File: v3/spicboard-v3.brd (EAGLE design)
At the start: 65 x 60 mm, 40 parts, among them IC1 74HC595, Q1 BC557, Q2 BC557

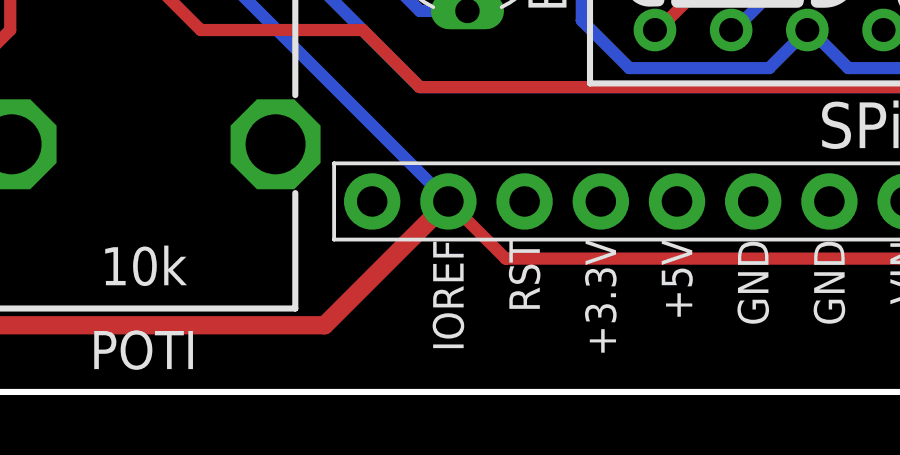
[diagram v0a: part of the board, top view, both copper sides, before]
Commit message: IOREF nach VCC umbenannt
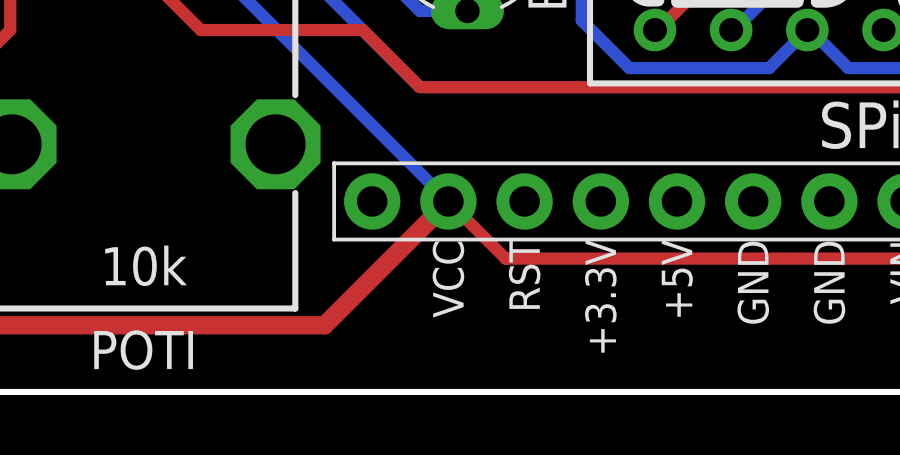
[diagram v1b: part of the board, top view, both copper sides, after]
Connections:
- net VCC: now also B1.VCC; no longer B1.IOREF
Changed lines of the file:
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@@
 <wire x1="2.794" y1="3.556" x2="4.1275" y2="2.2225" width="0.6096" layer="1"/>
 <wire x1="2.794" y1="3.556" x2="2.794" y2="4.191" width="0.6096" layer="1"/>
-<contactref element="B1" pad="IOREF"/>
+<contactref element="B1" pad="VCC"/>
 <wire x1="16.495" y1="15.255" x2="16.51" y2="15.24" width="0.4064" layer="16"/>
 <wire x1="16.51" y1="15.24" x2="16.51" y2="13.97" width="0.4064" layer="16"/>

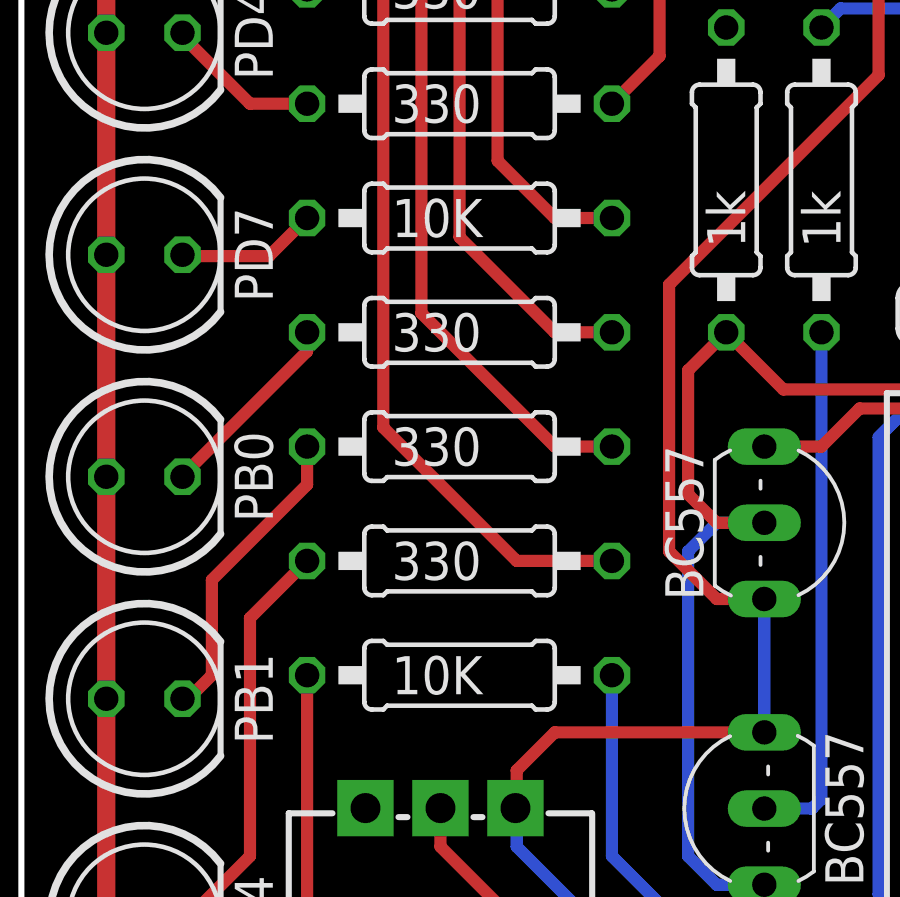
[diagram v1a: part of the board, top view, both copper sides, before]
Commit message: SPiCboard: 10K -> 10k
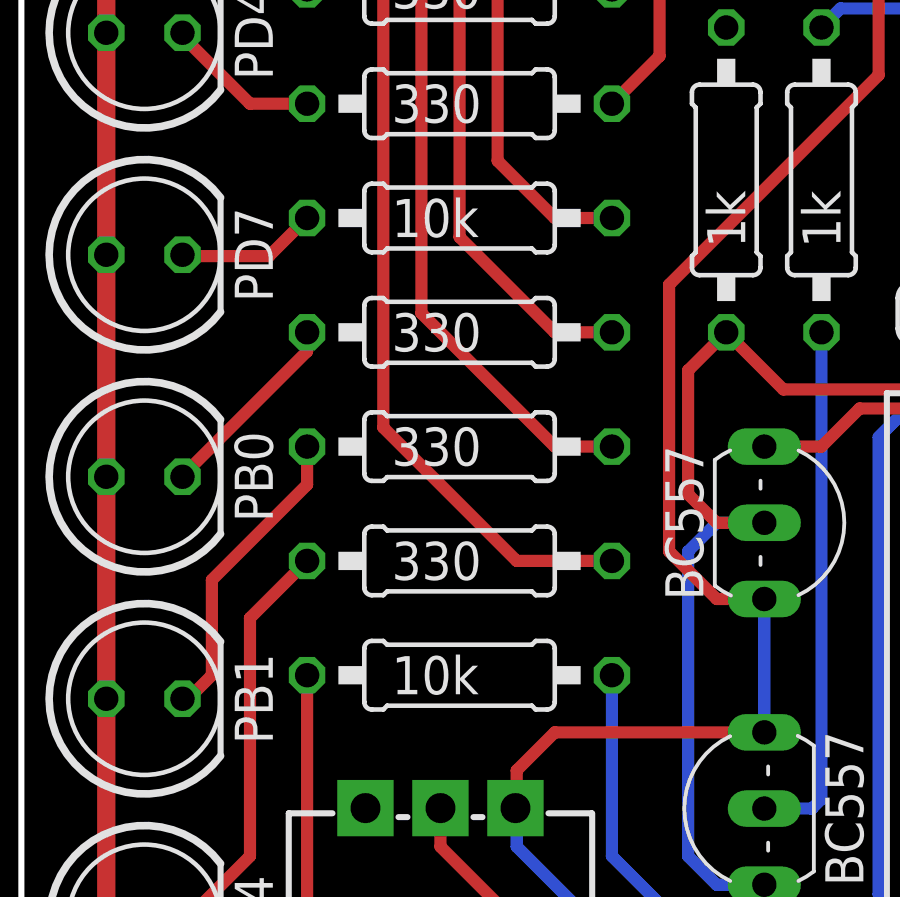
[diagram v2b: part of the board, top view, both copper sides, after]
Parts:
- R4, R8: value 10K -> 10k
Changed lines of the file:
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@@
 <attribute name="VALUE" x="12.3444" y="38.1" size="1.27" layer="25" ratio="10"/>
 </element>
-<element name="R4" library="resistor" package="0207/10" value="10K" x="14.605" y="34.925" smashed="yes">
+<element name="R4" library="resistor" package="0207/10" value="10k" x="14.605" y="34.925" smashed="yes">
 <attribute name="VALUE" x="12.3444" y="34.29" size="1.27" layer="25" ratio="10"/>
 </element>
@@
 <attribute name="VALUE" x="12.3444" y="22.86" size="1.27" layer="25" ratio="10"/>
 </element>
-<element name="R8" library="resistor" package="0207/10" value="10K" x="14.605" y="19.685" smashed="yes">
+<element name="R8" library="resistor" package="0207/10" value="10k" x="14.605" y="19.685" smashed="yes">
 <attribute name="VALUE" x="12.3444" y="19.05" size="1.27" layer="25" ratio="10"/>
 </element>

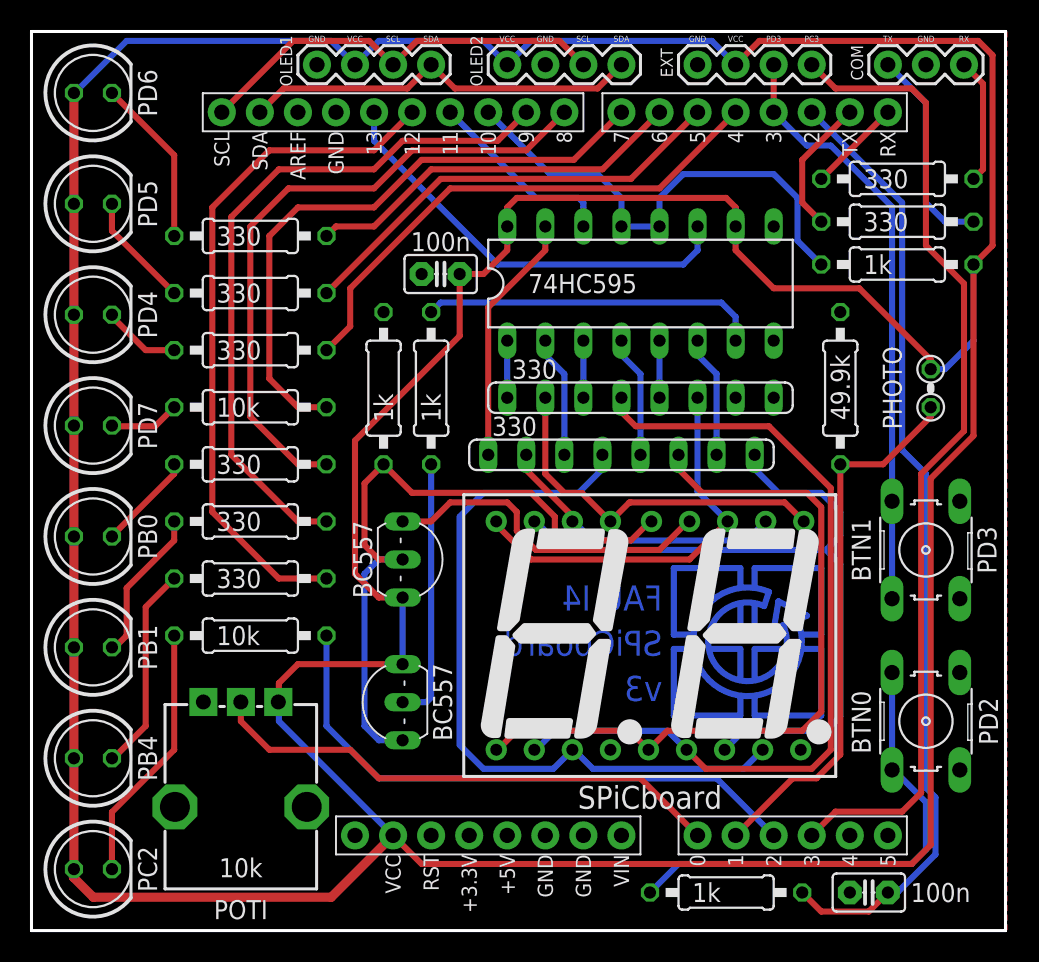
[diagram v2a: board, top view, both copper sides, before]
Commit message: LED Pin geaendert
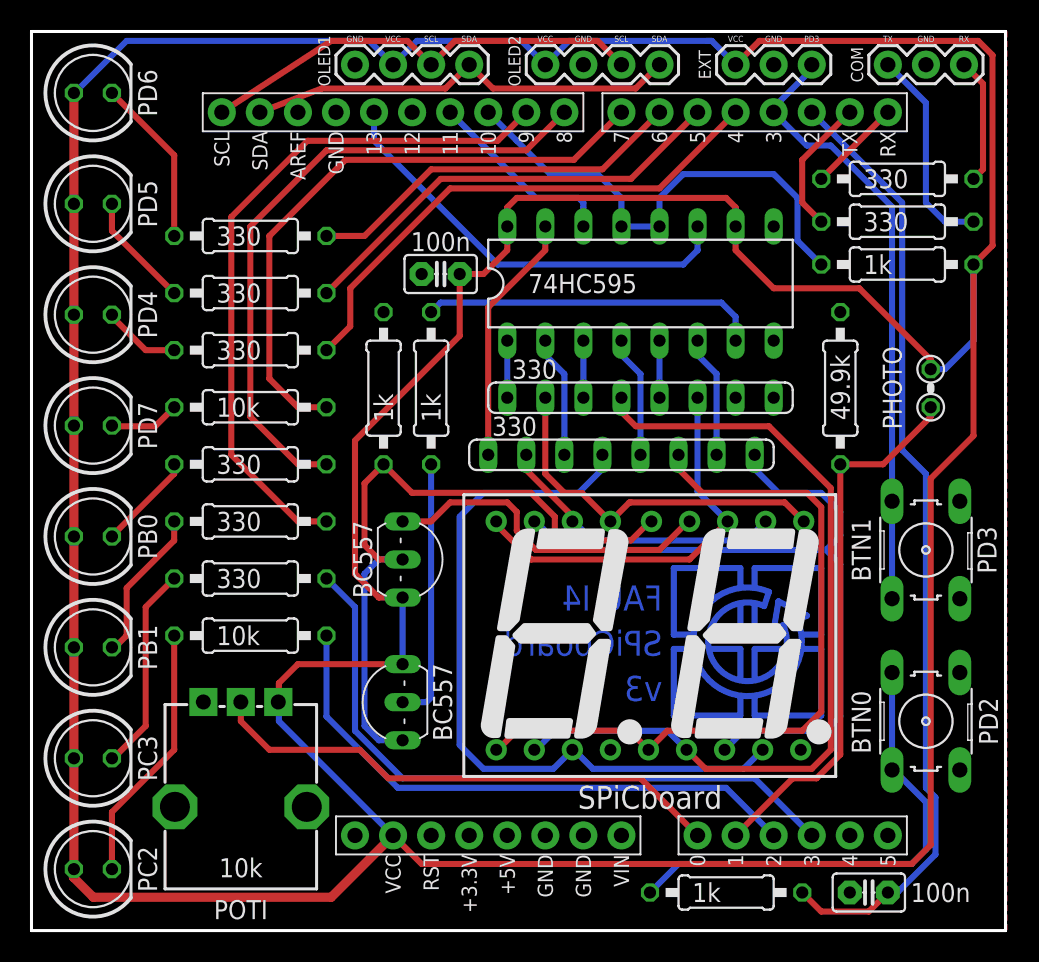
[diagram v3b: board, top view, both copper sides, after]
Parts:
- EXT: device SparkFun-Connectors:1X04 -> SparkFun-Connectors:1X03
- moved EXT 2.54 mm to (47.0, 57.8)
- moved OLED1 2.54 mm to (21.6, 57.8)
- moved OLED2 2.54 mm to (34.3, 57.8)
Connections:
- removed net EXTADC: B1.A3, EXT.4
- new net MISO: B1.D12, IC1.9
- net GND: now also EXT.2; no longer EXT.1
- net L6: now also B1.A3; no longer B1.D12
- net VCC: now also EXT.1; no longer EXT.2
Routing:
- net EXTADC: track 65.4 -> 0.00 mm
- net SDA: track 26.8 -> 28.9 mm
- net SCL: track 28.1 -> 30.1 mm
- net L6: track 45.7 -> 44.3 mm
- net BTN1: track 39.8 -> 40.9 mm
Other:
- board text removed: "PB4"

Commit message: SPiCboard: Bauteile ersetzt (PAD-Größe)
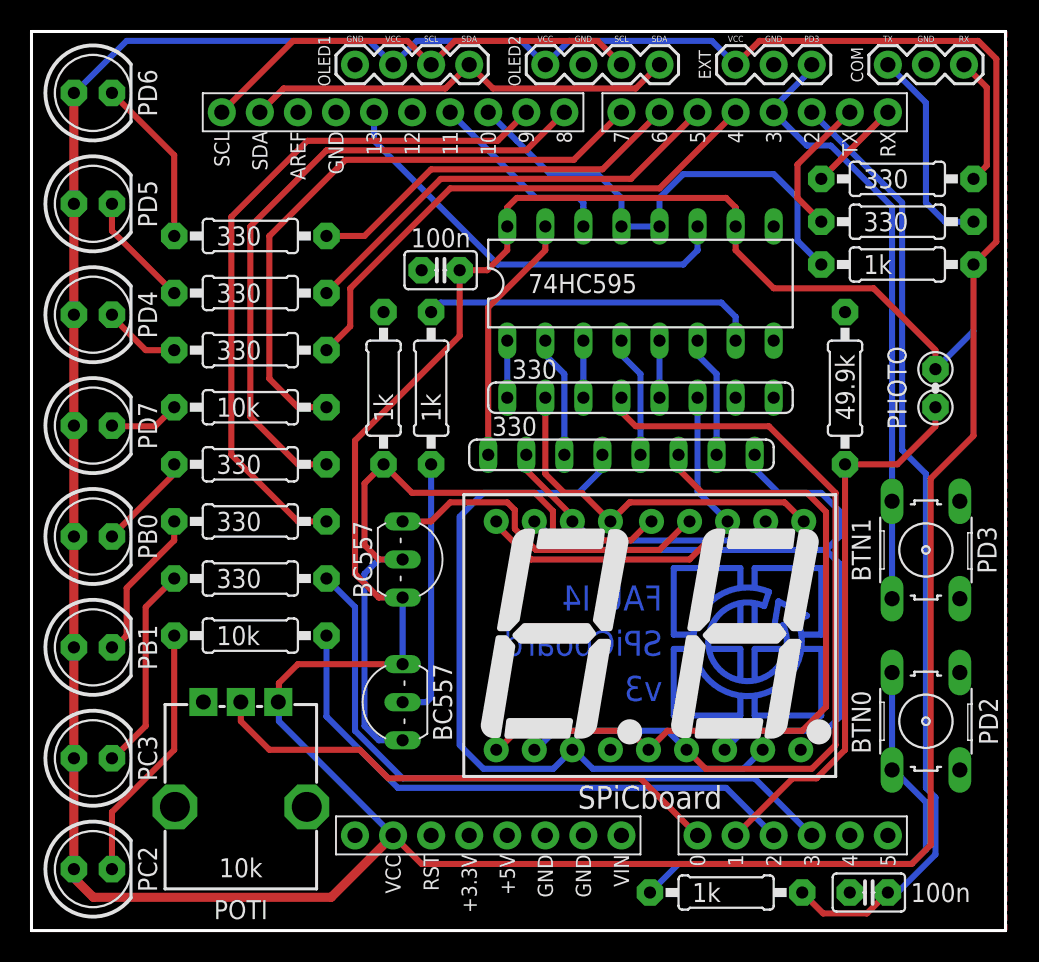
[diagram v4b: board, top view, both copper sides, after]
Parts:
- 7SEG: device display-kingbright:DA56 -> spicboard-v3:DA56
- BLUE0, BLUE1, GREEN0, GREEN1, RED0, RED1, YELLOW0, YELLOW1: device led:LED5MM -> spicboard-v3:LED5MM
- C1, C2: device capacitor-wima:C2.5-2 -> spicboard-v3:C2.5-2
- R1, R10, R11, R12, R13, R14, R15, R2, R3, R4, R5, R6, R7, R8, R9: device resistor:0207/10 -> spicboard-v3:0207/10
- moved PHOTO 0.32 mm to (60.3, 36.2)
- moved R10 0.32 mm to (54.3, 36.2)
- moved C1 0.25 mm to (27.3, 44.1)
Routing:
- net SCL: track 30.1 -> 30.6 mm
- net LDR: track 36.6 -> 37.1 mm

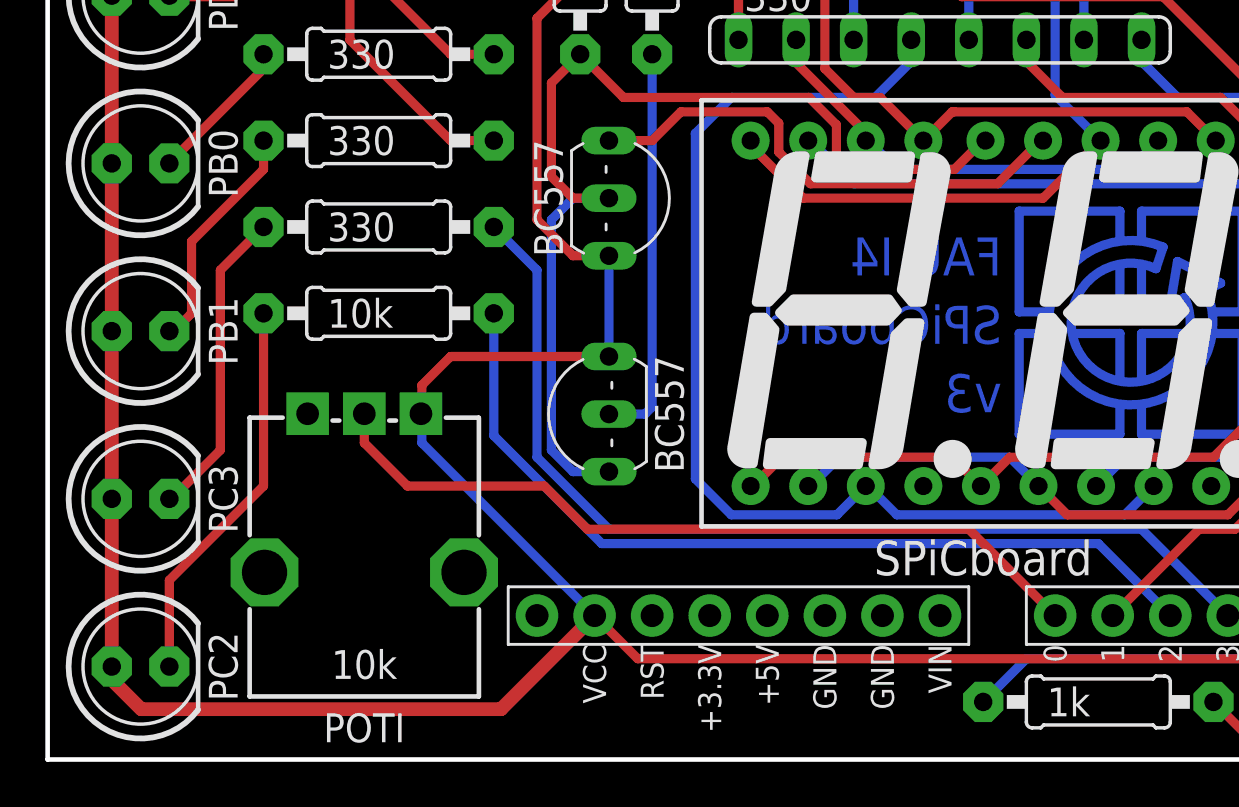
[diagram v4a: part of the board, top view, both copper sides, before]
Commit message: SPiCboard: Leitungen verschoben
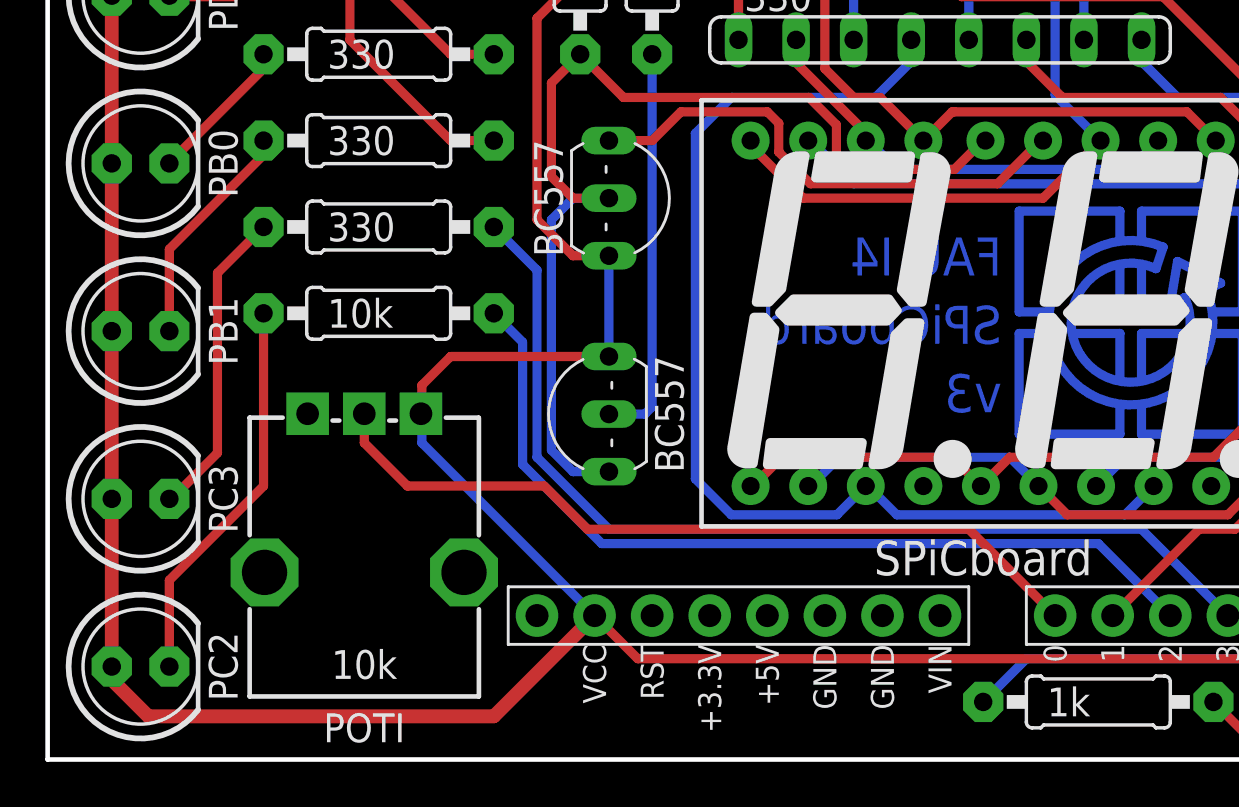
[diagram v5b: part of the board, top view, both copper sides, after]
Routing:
- net N$7: track 10.2 -> 10.8 mm
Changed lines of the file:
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@@
 <wire x1="2.83" y1="11.5" x2="2.83" y2="4.1" width="0.6096" layer="1"/>
 <wire x1="2.83" y1="18.9" x2="2.83" y2="11.5" width="0.6096" layer="1"/>
-<wire x1="4.1275" y1="2.2225" x2="20.0025" y2="2.2225" width="0.6096" layer="1"/>
+<wire x1="4.445" y1="1.905" x2="19.685" y2="1.905" width="0.6096" layer="1"/>
 <wire x1="24.765" y1="22.225" x2="24.765" y2="17.78" width="0.4064" layer="16"/>
 <contactref element="OLED1" pad="2"/>
@@
 <wire x1="63.1825" y1="59.3725" x2="48.5775" y2="59.3725" width="0.4064" layer="1"/>
 <wire x1="2.885" y1="4.1" x2="2.83" y2="4.1" width="0.4064" layer="1"/>
-<wire x1="2.794" y1="3.556" x2="4.1275" y2="2.2225" width="0.6096" layer="1"/>
+<wire x1="2.794" y1="3.556" x2="4.445" y2="1.905" width="0.6096" layer="1"/>
 <wire x1="2.794" y1="3.556" x2="2.794" y2="4.191" width="0.6096" layer="1"/>
 <contactref element="B1" pad="VCC"/>
@@
 <wire x1="16.51" y1="15.24" x2="16.51" y2="13.97" width="0.4064" layer="16"/>
 <wire x1="16.51" y1="13.97" x2="24.13" y2="6.35" width="0.4064" layer="16"/>
-<wire x1="20.0025" y1="2.2225" x2="24.13" y2="6.35" width="0.6096" layer="1"/>
+<wire x1="19.685" y1="1.905" x2="24.13" y2="6.35" width="0.6096" layer="1"/>
 <wire x1="24.765" y1="22.225" x2="23.1775" y2="22.225" width="0.4064" layer="1"/>
 <wire x1="23.1775" y1="22.225" x2="21.59" y2="23.8125" width="0.4064" layer="1"/>
@@
 <contactref element="YELLOW1" pad="K"/>
 <contactref element="R6" pad="1"/>
-<wire x1="5.37" y1="18.9" x2="5.565" y2="18.9" width="0.4064" layer="1"/>
-<wire x1="5.565" y1="18.9" x2="6.35" y2="19.685" width="0.4064" layer="1"/>
-<wire x1="6.35" y1="19.685" x2="6.35" y2="22.86" width="0.4064" layer="1"/>
-<wire x1="6.35" y1="22.86" x2="9.525" y2="26.035" width="0.4064" layer="1"/>
-<wire x1="9.525" y1="26.035" x2="9.525" y2="27.305" width="0.4064" layer="1"/>
+<wire x1="9.525" y1="27.305" x2="9.525" y2="26.67" width="0.4064" layer="1"/>
+<wire x1="9.525" y1="27.305" x2="9.525" y2="26.67" width="0.4064" layer="1"/>
+<wire x1="5.37" y1="22.515" x2="5.37" y2="18.9" width="0.4064" layer="1"/>
+<wire x1="9.525" y1="26.67" x2="5.37" y2="22.515" width="0.4064" layer="1"/>
 </signal>
 <signal name="N$8">
@@
 <contactref element="R7" pad="1"/>
 <wire x1="5.37" y1="11.5" x2="5.4675" y2="11.5" width="0.4064" layer="1"/>
-<wire x1="5.4675" y1="11.5" x2="7.62" y2="13.6525" width="0.4064" layer="1"/>
-<wire x1="7.62" y1="13.6525" x2="7.62" y2="21.59" width="0.4064" layer="1"/>
-<wire x1="7.62" y1="21.59" x2="9.525" y2="23.495" width="0.4064" layer="1"/>
+<wire x1="5.4675" y1="11.5" x2="7.493" y2="13.5255" width="0.4064" layer="1"/>
+<wire x1="7.493" y1="13.5255" x2="7.493" y2="21.463" width="0.4064" layer="1"/>
+<wire x1="7.493" y1="21.463" x2="9.525" y2="23.495" width="0.4064" layer="1"/>
 </signal>
 <signal name="N$9">
@@
 <contactref element="R8" pad="2"/>
 <contactref element="B1" pad="A2"/>
-<wire x1="19.685" y1="19.685" x2="19.685" y2="14.2875" width="0.4064" layer="16"/>
-<wire x1="19.685" y1="14.2875" x2="24.4475" y2="9.525" width="0.4064" layer="16"/>
-<wire x1="24.4475" y1="9.525" x2="46.355" y2="9.525" width="0.4064" layer="16"/>
+<wire x1="46.355" y1="9.525" x2="24.4475" y2="9.525" width="0.4064" layer="16"/>
 <wire x1="46.355" y1="9.525" x2="49.53" y2="6.35" width="0.4064" layer="16"/>
+<wire x1="24.4475" y1="9.525" x2="20.955" y2="13.0175" width="0.4064" layer="16"/>
+<wire x1="20.955" y1="13.0175" x2="20.955" y2="18.415" width="0.4064" layer="16"/>
+<wire x1="20.955" y1="18.415" x2="19.685" y2="19.685" width="0.4064" layer="16"/>
 </signal>
 <signal name="N$17">
